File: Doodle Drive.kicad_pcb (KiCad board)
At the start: 2 copper layers, 97.8 x 99.1 mm, 142 parts, among them J1 USB_B, J12 PINHD_1x4_Male, J15 PINHD_1x4_Male, J2 PINHD_1x4_Male, J6 PINHD_1x2_Male, J8 PINHD_1x4_Male, J9 PINHD_1x4_Male, SW1 Push_Button, SW2 Push_Button, SW3 Push_Button, U1 STM32F411RETx, U2 DRV8825PWP, U3 DRV8825PWP, U4 DRV8825PWP, U5 DRV8825PWP, U6 AP7343-30W5-7, U7 CP2102N-Axx-xQFN28, Y1 32.768KHz ±20ppm 12.5pF, Y2 25MHZ 9PF

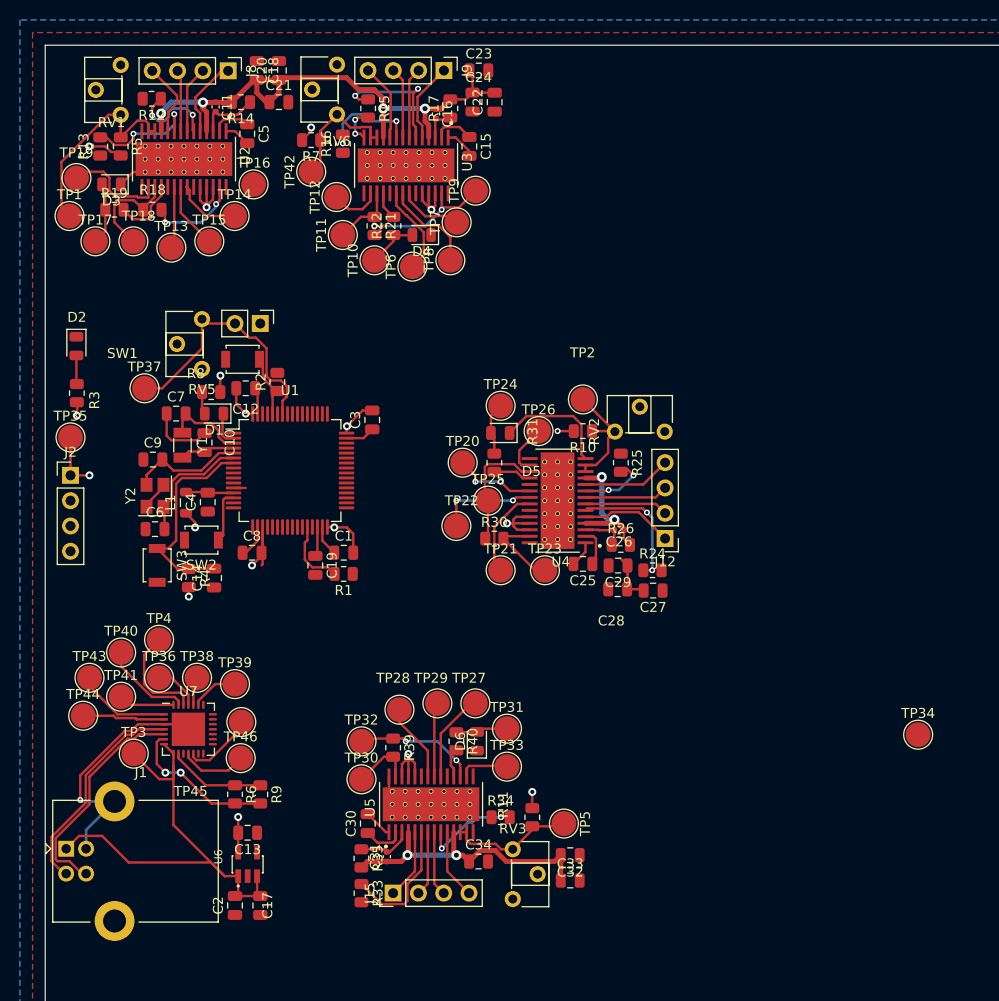
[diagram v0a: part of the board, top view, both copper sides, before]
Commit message: moved stuff closer, changed testpoint footprint, connected VM
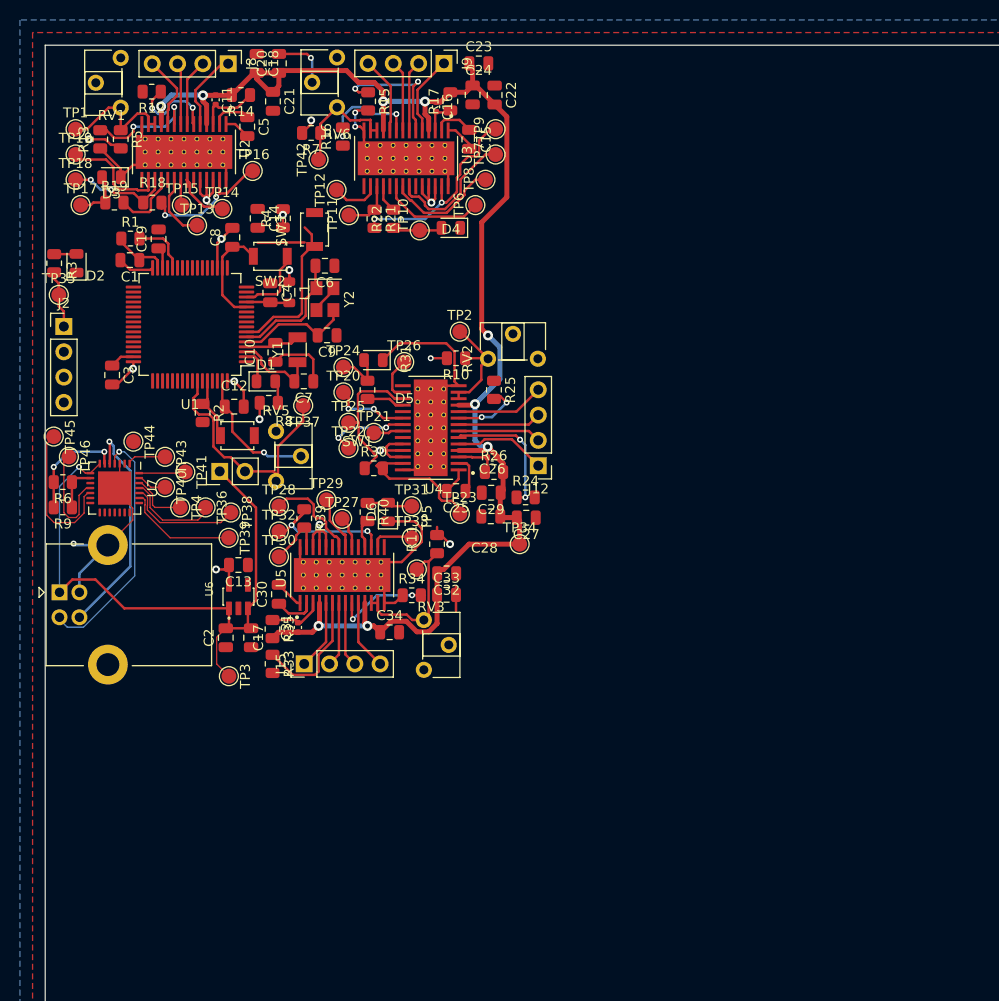
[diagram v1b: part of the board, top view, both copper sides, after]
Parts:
- TP1, TP10, TP11, TP12, TP13, TP14, TP15, TP16, TP17, TP18, TP19, TP2, TP20, TP21, TP22, TP23, TP24, TP25, TP26, TP27, TP28, TP29, TP3, TP30, TP31, TP32, TP33, TP34, TP35, TP36, TP37, TP38, TP39, TP4, TP40, TP41, TP42, TP43, TP44, TP45, TP46, TP5, TP6, TP7, TP8, TP9: footprint TestPoint:TestPoint_Pad_D2.5mm -> TestPoint:TestPoint_Pad_D1.5mm
- moved TP34 44.3 mm to (47.6, -49.0)
- moved R1 39.9 mm to (8.55, -79.7), turned to 0 degrees
- moved R4 37.3 mm to (23.9, -81.7), turned to 90 degrees
- moved SW3 37.2 mm to (27.0, -80.6), turned to 90 degrees
- moved C1 36.4 mm to (8.50, -77.5), turned to 180 degrees
- moved C14 36.4 mm to (21.3, -81.7), turned to -90 degrees
- moved C19 36.4 mm to (11.4, -79.6), turned to 90 degrees
- moved R6 35.8 mm to (1.77, -55.2), turned to 180 degrees
- moved R9 35.0 mm to (1.77, -52.7), turned to 180 degrees
- moved TP46 34.8 mm to (2.38, -57.7), turned to -90 degrees
- moved TP45 34.3 mm to (0.85, -59.8), turned to -90 degrees
- moved C8 31.7 mm to (18.8, -79.8), turned to 90 degrees
- moved C6 31.5 mm to (28.1, -76.9), turned to 180 degrees
- moved C33 31.2 mm to (40.3, -43.9)
- moved C32 30.9 mm to (40.3, -46.0)
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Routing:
- net GND: track 68.7 -> 117.4 mm, vias 3 -> 5
- net +15V: track 104.0 -> 152.1 mm, vias 8 -> 9
- net +5V: track 48.3 -> 62.9 mm, vias 0 -> 1
- net NRTS: track 2.87 -> 11.6 mm
- net NRI: track 8.26 -> 0.00 mm
- net Net-(U2-AVREF): track 20.9 -> 12.7 mm
- net PC12: track 7.24 -> 15.1 mm
- net PA2: track 6.39 -> 13.4 mm
- net NCTS: track 4.77 -> 11.4 mm
- net PB5: track 9.13 -> 3.03 mm
- net NDSR: track 8.98 -> 2.98 mm
- net DIR4: track 9.02 -> 3.24 mm
- net NHOME3: track 8.22 -> 14.0 mm
- net NDCD: track 9.50 -> 3.95 mm
- net +3V3: track 69.5 -> 64.1 mm, vias 18 -> 15
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
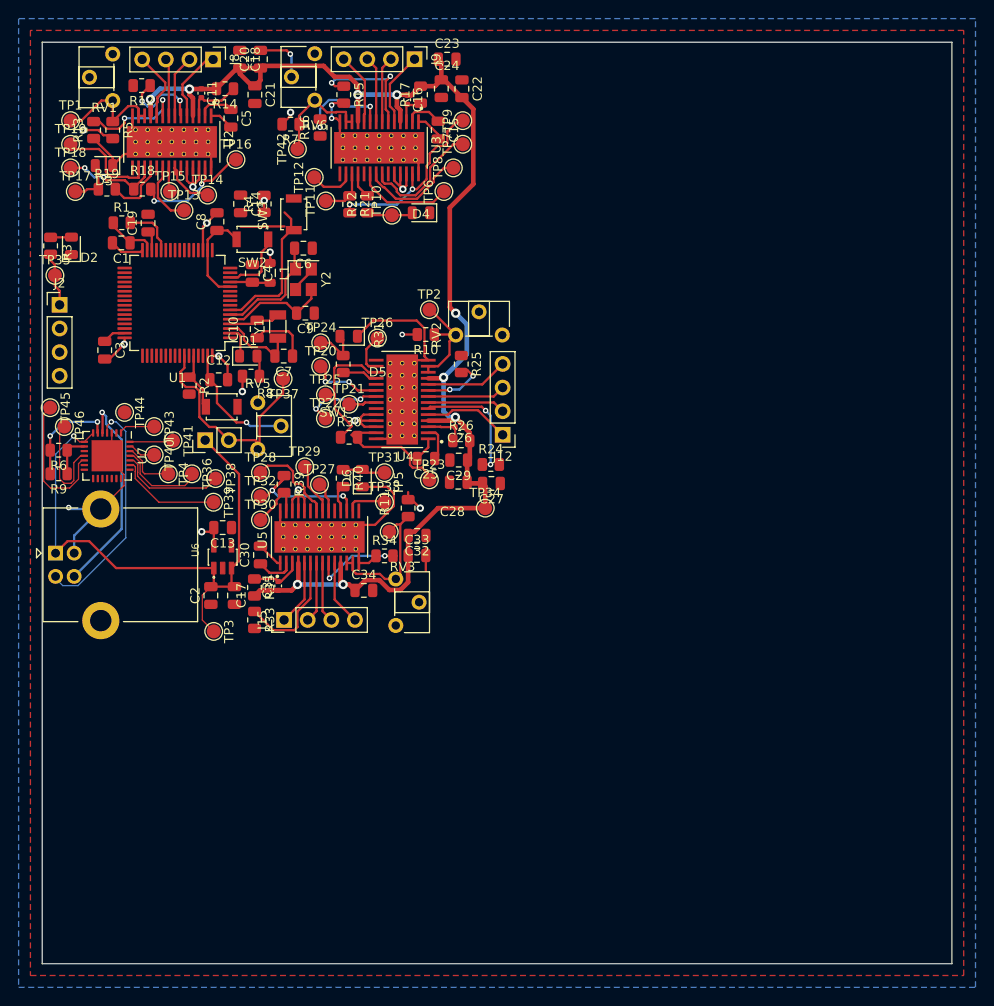
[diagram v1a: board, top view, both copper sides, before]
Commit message: finished PCB. DRC 0 errors
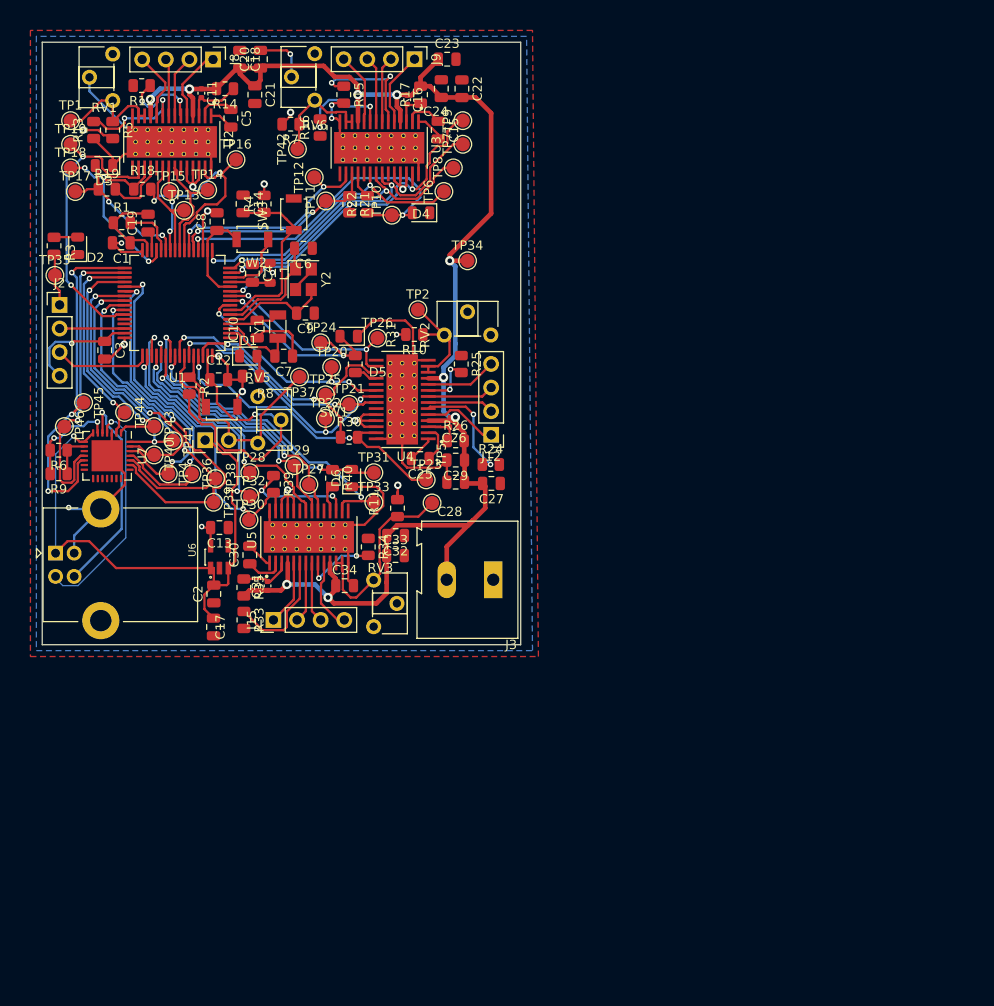
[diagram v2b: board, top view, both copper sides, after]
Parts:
- removed TP3: TestPoint, TestPoint:TestPoint_Pad_D1.5mm
- added J3: Screw_Terminal_01x02, TerminalBlock:TerminalBlock_Altech_AK300-2_P5.00mm, F.Cu at (48.5, -41.3)
- moved TP34 26.7 mm to (45.7, -75.6)
- moved TP5 5.55 mm to (41.9, -49.5)
- moved C17 4.07 mm to (18.4, -36.2)
- moved TP45 3.63 mm to (4.45, -60.3)
- moved RV3 2.38 mm to (35.6, -41.2)
- moved C32 2.31 mm to (38.0, -46.0)
- moved C33 2.31 mm to (38.0, -43.9)
- moved C34 2.13 mm to (32.5, -40.6)
- moved R34 1.99 mm to (35.0, -44.8), turned to -90 degrees
- moved TP37 1.78 mm to (27.7, -63.1)
- moved R31 1.30 mm to (33.7, -64.5)
- moved J12 1.23 mm to (48.3, -56.9)
- moved R10 1.23 mm to (40.0, -67.6)
- moved RV2 1.23 mm to (43.2, -67.6)
- moved TP2 1.23 mm to (40.4, -70.3)
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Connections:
- TP14 pad 1: PA9 -> PC4
- TP28 pad 1: PB14 -> PC11
- TP45 pad 1: PC12 -> PB12
- TP7 pad 1: PA2 -> PA1
- U1 pad 10: NSLEEP4 -> NRESET3
- U1 pad 11: NRESET4 -> NHOME1
- U1 pad 15: DIR1 -> PA1
- U1 pad 16: PA2 -> NENBL1
- U1 pad 17: NENBL1 -> DIR1
- U1 pad 20: NHOME1 -> NFAULT1
- U1 pad 21: NFAULT1 -> NSLEEP1
- U1 pad 22: NSLEEP1 -> NRESET1
- U1 pad 23: NRESET1 -> NHOME2
- U1 pad 24: NRTS -> PC4
- U1 pad 25: NCTS -> DIR2
- U1 pad 26: NFAULT2 -> NENBL2
- U1 pad 27: NSLEEP2 -> NFAULT2
- U1 pad 29: NSLEEP3 -> NSLEEP2
- U1 pad 33: NRESET3 -> PB12
- U1 pad 34: DIR4 -> NSUSPEND
- U1 pad 35: PB14 -> NRI
- U1 pad 36: NENBL4 -> NDCD
- U1 pad 39: NDSR -> NDTR
- U1 pad 40: NDTR -> NDSR
- U1 pad 41: DIR2 -> NRTS
- U1 pad 42: PA9 -> NCTS
- U1 pad 43: NENBL2 -> NRESET2
- U1 pad 50: NHOME2 -> NHOME4
- U1 pad 51: NDCD -> NSLEEP4
- U1 pad 52: NRI -> PC11
- U1 pad 53: PC12 -> NENBL4
- U1 pad 54: NSUSPEND -> DIR4
- U1 pad 55: NRESET2 -> NFAULT4
- U1 pad 56: DIR3 -> NRESET4
- U1 pad 62: NFAULT3 -> NSLEEP3
- U1 pad 8: NHOME4 -> DIR3
- U1 pad 9: NFAULT4 -> NFAULT3
- U2 pad 22: PA9 -> PC4
- U3 pad 22: PA2 -> PA1
- U5 pad 22: PB14 -> PC11
- U7 pad 12: PC12 -> PB12
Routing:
- net GND: track 117.4 -> 174.8 mm, vias 5 -> 6
- net PB12: track 0.00 -> 39.2 mm, vias 0 -> 3
- net PA1: track 0.00 -> 35.5 mm, vias 0 -> 2
- net NFAULT1: track 5.04 -> 37.1 mm, vias 0 -> 2
- net PC11: track 0.00 -> 28.7 mm, vias 0 -> 2
- net NRESET4: track 4.37 -> 33.0 mm, vias 0 -> 2
- net NCTS: track 11.4 -> 39.9 mm, vias 0 -> 2
- net NFAULT4: track 5.10 -> 33.5 mm, vias 0 -> 2
- net NSLEEP4: track 15.1 -> 42.0 mm, vias 2 -> 4
- net NDSR: track 2.98 -> 29.9 mm, vias 0 -> 2
- net NRTS: track 11.6 -> 37.8 mm, vias 0 -> 2
- net PC6: track 9.56 -> 35.2 mm, vias 0 -> 2
- net PC7: track 5.79 -> 31.4 mm, vias 0 -> 2
- net NHOME4: track 6.06 -> 31.1 mm, vias 0 -> 2
- net NENBL4: track 5.62 -> 30.6 mm, vias 0 -> 2
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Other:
- board size 97.8 x 99.1 mm -> 51.4 x 64.8 mm

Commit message: last polishing on pcb v1. ich isch abgabe dc
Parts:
- moved J3 35.2 mm to (43.8, -76.1), turned to -90 degrees
- moved RV2 9.02 mm to (35.6, -72.4), turned to 180 degrees
- moved TP10 8.57 mm to (45.7, -83.2)
- moved TP34 5.68 mm to (48.3, -80.6)
- moved TP2 4.85 mm to (35.6, -69.8)
- moved R10 4.55 mm to (44.5, -66.7), turned to 0 degrees
- moved D4 1.98 mm to (38.7, -80.7)
- moved R25 0.96 mm to (45.1, -63.5)
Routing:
- net +15V: track 166.0 -> 217.4 mm, vias 9 -> 10
- net NFAULT1: track 37.1 -> 48.5 mm, vias 2 -> 3
- net Net-(U4-AVREF): track 12.0 -> 16.7 mm
- net GND: track 174.8 -> 172.8 mm, vias 6 -> 5
- net Net-(U4-ISENB): track 5.86 -> 4.36 mm, vias 2 -> 0
- net +3V3: track 68.4 -> 69.6 mm
- net Net-(J1-D-): track 25.0 -> 25.9 mm
- net NHOME3: track 33.7 -> 34.6 mm
- net NDCD: track 26.5 -> 27.3 mm
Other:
- board size 51.4 x 64.8 mm -> 50.2 x 64.8 mm

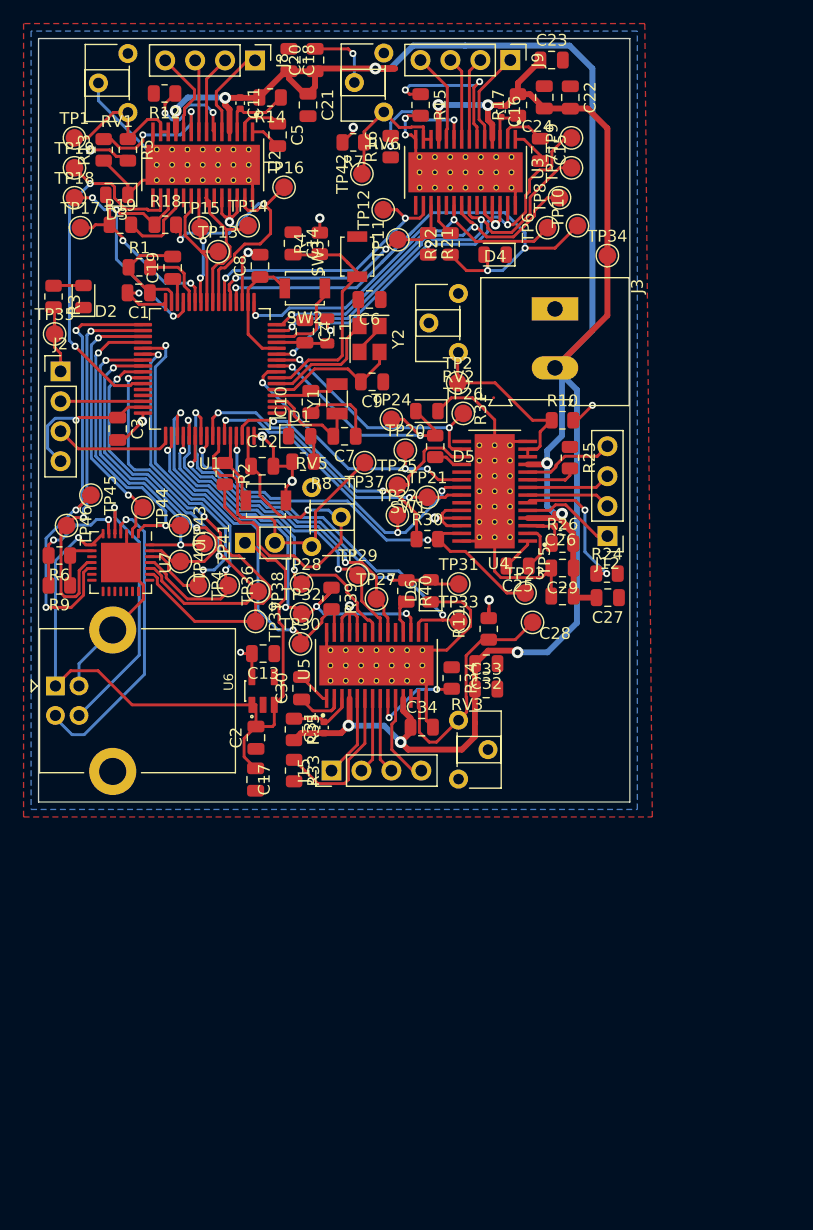
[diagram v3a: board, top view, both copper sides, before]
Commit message: completly reroutet EVERYTHING
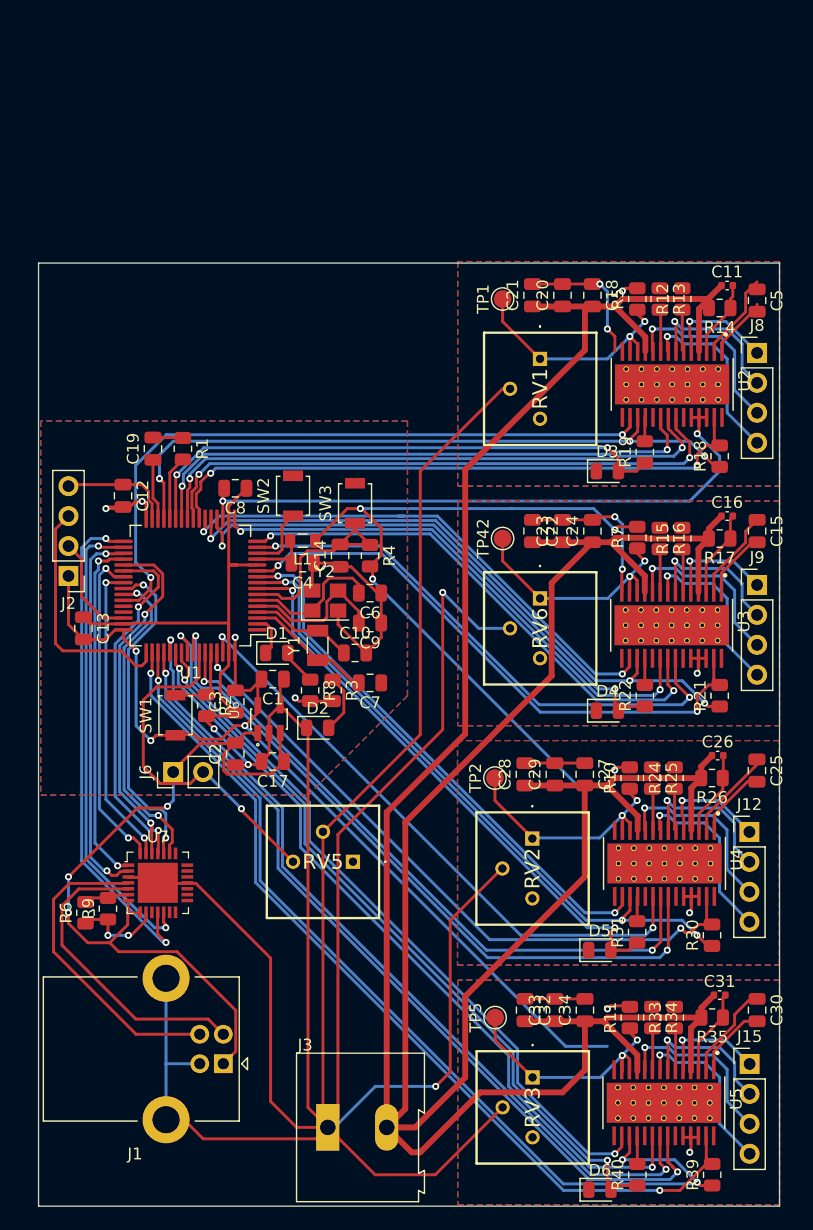
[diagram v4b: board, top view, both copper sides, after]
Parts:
- removed TP10, TP11, TP12, TP13, TP14, TP15, TP16, TP17, TP18, TP19, TP20, TP21, TP22, TP23, TP24, TP25, TP26, TP27, TP28, TP29, TP30, TP31, TP32, TP33, TP34, TP35, TP36, TP37, TP38, TP39, TP4, TP40, TP41, TP43, TP44, TP45, TP46, TP6, TP7, TP8, TP9: TestPoint, TestPoint:TestPoint_Pad_D1.5mm
- RV1, RV2, RV3, RV5, RV6: footprint Potentiometer_THT:Potentiometer_ACP_CA6-H2,5_Horizontal -> poti:3386P1473LF
- U7: value CP2102N-Axx-xQFN28 -> CP2102-GMR_NRND; footprint Package_DFN_QFN:QFN-28-1EP_5x5mm_P0.5mm_EP3.35x3.35mm -> digikey-footprints:VFQFN-28-1EP_5x5mm
- moved J3 72.1 mm to (24.5, -6.68), turned to 0 degrees
- moved R39 58.6 mm to (57.1, -2.67), turned to 90 degrees
- moved R40 53.3 mm to (50.8, -2.67), turned to 90 degrees
- moved D6 52.8 mm to (47.6, -1.40), turned to 0 degrees
- moved R18 51.0 mm to (57.8, -63.6), turned to 90 degrees
- moved J8 49.3 mm to (61.0, -72.4), turned to 0 degrees
- moved J9 49.2 mm to (61.0, -52.7), turned to 0 degrees
- moved R13 48.8 mm to (52.7, -77.0), turned to -90 degrees
- moved R19 48.5 mm to (51.4, -64.0), turned to 90 degrees
- moved D5 48.0 mm to (47.6, -21.7), turned to 0 degrees
- moved D3 47.8 mm to (48.3, -62.4), turned to 0 degrees
- moved C30 47.3 mm to (61.0, -16.6), turned to -90 degrees
- moved R12 47.3 mm to (54.6, -77.0), turned to 90 degrees
- moved R21 45.6 mm to (57.8, -43.3), turned to 90 degrees
- moved R5 45.0 mm to (50.8, -77.0), turned to 90 degrees
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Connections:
- net NCTS renamed PA9
- net NDCD renamed PB15
- net NDSR renamed PC9
- net NDTR renamed PC8
- net NENBL1 renamed PA2
- net NENBL3 renamed PB7
- net NENBL4 renamed PC12
- net NFAULT1 renamed PA4
- net NFAULT2 renamed PB1
- net NFAULT4 renamed PB3
- net NHOME1 renamed PC3
- net NHOME2 renamed PA7
- net NHOME3 renamed PB8
- net NHOME4 renamed PA15
- net NRESET1 renamed PA6
- net NRESET2 renamed PA10
- net NRESET3 renamed PC2
- net NRESET4 renamed PB4
- net NRI renamed PB14
- net NRST renamed ~{RST}
- net NRTS renamed PA8
- net NSLEEP1 renamed PA5
- net NSLEEP2 renamed PB10
- net NSLEEP4 renamed PC10
- D5 pad 2: NFAULT3 -> PC0
- J12 pad 3: Net-(U4-BOUT2) -> Net-(U4-BOUT1)
- J12 pad 4: Net-(U4-BOUT1) -> Net-(U4-BOUT2)
- J15 pad 3: Net-(U5-BOUT2) -> Net-(U5-BOUT1)
- J15 pad 4: Net-(U5-BOUT1) -> Net-(U5-BOUT2)
- J8 pad 3: Net-(U2-BOUT2) -> Net-(U2-BOUT1)
- J8 pad 4: Net-(U2-BOUT1) -> Net-(U2-BOUT2)
- J9 pad 3: Net-(U3-BOUT2) -> Net-(U3-BOUT1)
- J9 pad 4: Net-(U3-BOUT1) -> Net-(U3-BOUT2)
- R30 pad 1: NSLEEP3 -> PC1
- R31 pad 1: NFAULT3 -> PC0
- U1 pad 25: DIR2 -> PC5
- U1 pad 26: NENBL2 -> DIR2
- U1 pad 34: NSUSPEND -> PB13
- U1 pad 62: NSLEEP3 -> DIR3
- U1 pad 8: DIR3 -> PC0
- U1 pad 9: NFAULT3 -> PC1
- U2 pad 21: NENBL2 -> PC5
- U4 pad 17: NSLEEP3 -> PC1
- U7 pad 11: NSUSPEND -> PB12
- U7 pad 12: PB12 -> PB13
- U7 pad 18: unconnected-(U7-~{RXT}/GPIO.1-Pad18) -> GND
- U7 pad 25: PC6 -> PC7
- U7 pad 26: PC7 -> PC6
- U7 pad 4: Net-(J1-D-) -> Net-(J1-D+)
- U7 pad 5: Net-(J1-D+) -> Net-(J1-D-)
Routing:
- net GND: track 172.8 -> 407.9 mm, vias 5 -> 8
- net +3V3: track 69.6 -> 221.9 mm, vias 16 -> 18
- net +15V: track 217.4 -> 304.9 mm, vias 10 -> 0
- net PC1: track 0.00 -> 55.9 mm, vias 0 -> 3
- net PC5: track 0.00 -> 49.6 mm, vias 0 -> 2
- net PC0: track 0.00 -> 49.0 mm, vias 0 -> 2
- net PA15: track 30.9 -> 76.1 mm
- net PC11: track 28.7 -> 70.8 mm
- net PC12: track 30.6 -> 70.7 mm
- net PB13: track 0.00 -> 40.1 mm, vias 0 -> 2
- net PC10: track 41.9 -> 81.4 mm, vias 4 -> 3
- net DIR4: track 27.9 -> 66.2 mm
- net PC4: track 12.6 -> 50.2 mm, vias 0 -> 2
- net DIR2: track 11.2 -> 48.7 mm, vias 0 -> 2
- net PB5: track 25.9 -> 60.0 mm
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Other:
- board size 50.2 x 64.8 mm -> 62.9 x 80 mm
